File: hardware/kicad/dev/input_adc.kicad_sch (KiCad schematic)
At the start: 90 parts, among them J101 BNC_Rosenberger, J101/2 Conn_01x01_Shielded, SW101 SW_DIP_x04, SW102 SW_DIP_x03, SW103 SW_DIP_x04, SW104 SW_DIP_x03, U101 AD8138ARZ, U102 AD9235

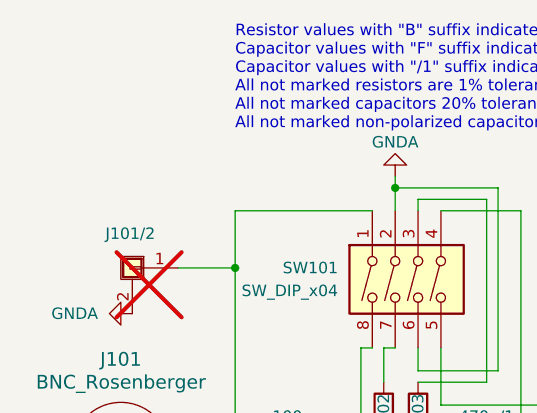
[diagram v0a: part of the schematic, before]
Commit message: repositioning of parts for more case options
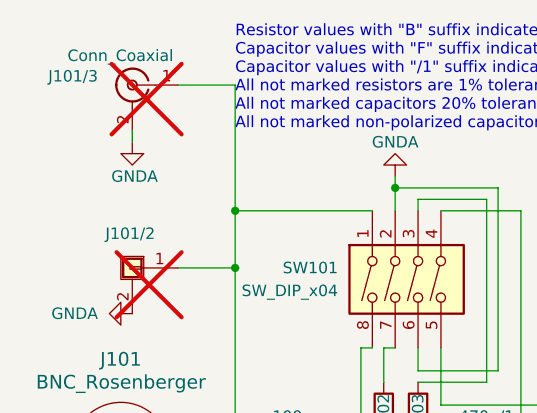
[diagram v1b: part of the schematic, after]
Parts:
- added J101/3: Conn_Coaxial, Connector_Coaxial:BNC_Amphenol_B6252HB-NPP3G-50_Horizontal, symbol Connector:Conn_Coaxial
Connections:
- net GNDA: now also J101/3.2 (Ext)
- net at C101.1, J101.1 (Signal), J101/2.1 (Pin_1)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: now also J101/3.1 (In)
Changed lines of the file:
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@@
 	)
 	(junction
+		(at 35.56 36.83)
+		(diameter 0)
+		(color 0 0 0 0)
+	)
+	(junction
 		(at 127 91.44)
 		(diameter 0)
@@
 	(wire
 		(pts
+			(xy 29.21 22.86) (xy 35.56 22.86)
+		)
+		(stroke
+			(width 0)
+			(type default)
+		)
+	)
+	(wire
+		(pts
 			(xy 49.53 63.5) (xy 52.07 63.5)
 		)
@@
 	(wire
 		(pts
+			(xy 24.13 27.94) (xy 24.13 29.21)
+		)
+		(stroke
+			(width 0)
+			(type default)
+		)
+	)
+	(wire
+		(pts
 			(xy 58.42 59.69) (xy 67.31 59.69)
 		)
@@
 	(wire
 		(pts
+			(xy 35.56 22.86) (xy 35.56 36.83)
+		)
+		(stroke
+			(width 0)
+			(type default)
+		)
+	)
+	(wire
+		(pts
 			(xy 129.54 30.48) (xy 129.54 43.18)
 		)
@@
 	)
 	(symbol
+		(lib_id "Connector:Conn_Coaxial")
+		(at 24.13 22.86 0)
+		(mirror y)
+		(unit 1)
+		(exclude_from_sim no)
+		(in_bom yes)
+		(on_board yes)
+		(dnp yes)
+		(property "Reference" "J101/3"
+			(at 20.32 21.8831 0)
+			(effects
+				(font
+					(size 1.27 1.27)
+				)
+				(justify left)
+			)
+		)
+		(property "Value" "Conn_Coaxial"
+			(at 28.702 19.5971 0)
+			(effects
+				(font
+					(size 1.27 1.27)
+				)
+				(justify left)
+			)
+		)
+		(property "Footprint" "Connector_Coaxial:BNC_Amphenol_B6252HB-NPP3G-50_Horizontal"
+			(at 24.13 22.86 0)
+			(effects
+				(font
+					(size 1.27 1.27)
+				)
+				(hide yes)
+			)
+		)
+		(property "Datasheet" "~"
+			(at 24.13 22.86 0)
+			(effects
+				(font
+					(size 1.27 1.27)
+				)
+				(hide yes)
+			)
+		)
+		(property "Description" "coaxial connector (BNC, SMA, SMB, SMC, Cinch/RCA, LEMO, ...)"
+			(at 24.13 22.86 0)
+			(effects
+				(font
+					(size 1.27 1.27)
+				)
+				(hide yes)
+			)
+		)
+		(pin "2"
+		)
+		(pin "1"
+		)
+		(instances
+			(project "misrc_v2.5"
+				(path "/bc796fa4-76ff-4554-a44c-2597c6c5788e/f3827713-3b6b-4193-bf1c-3910c26c6fe9"
+					(reference "J101/3")
+					(unit 1)
+				)
+			)
+		)
+	)
+	(symbol
 		(lib_id "Device:C")
 		(at 213.36 39.37 0)
@@
 					(unit 1)
 				)
+			)
+		)
+	)
+	(symbol
+		(lib_id "power:GNDA")
+		(at 24.13 29.21 0)
+		(unit 1)
+		(exclude_from_sim no)
+		(in_bom yes)
+		(on_board yes)
+		(dnp no)
+		(property "Reference" "#PWR017"
+			(at 24.13 35.56 0)
+			(effects
+				(font
+					(size 1.27 1.27)
+				)
+				(hide yes)
+			)
+		)
+		(property "Value" "GNDA"
+			(at 24.384 33.02 0)
+			(effects
+				(font
+					(size 1.27 1.27)
+				)
+			)
+		)
+		(property "Footprint" ""
+			(at 24.13 29.21 0)
+			(effects
+				(font
+					(size 1.27 1.27)
+				)
+				(hide yes)
+			)
+		)
+		(property "Datasheet" ""
+			(at 24.13 29.21 0)
+			(effects
+				(font
+					(size 1.27 1.27)
+				)
+				(hide yes)
+			)
+		)
+		(property "Description" ""
+			(at 24.13 29.21 0)
+			(effects
+				(font
+					(size 1.27 1.27)
+				)
+				(hide yes)
+			)
+		)
+		(pin "1"
+		)
+		(instances
+			(project "misrc_v2.5"
+				(path "/bc796fa4-76ff-4554-a44c-2597c6c5788e/f3827713-3b6b-4193-bf1c-3910c26c6fe9"
+					(reference "#PWR017")
+					(unit 1)
+				)
